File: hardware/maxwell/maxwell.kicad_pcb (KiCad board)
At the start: 2 copper layers, 124 x 60 mm, 81 parts, among them J1 Canbus 1, J10 SPI2_B, J11 BACKUP, J12 UART4, J13 UART5, J14 I2C1, J15 GPIO, J16 ESP_BM, J17 ESP_PROG, J18 Supercap, J2 Canbus 2, J3 Neopixel, J4 BOOT0, J5 SPI2_A, J6 Programmer, J7 Dynamo Input, J8 BOOT1, J9 Battery, Q1 BSS138, Q2 PSMN5R4-25YLD, Q3 NTR1P02T1, Q4 NTR1P02T1, Q5 NTR1P02T1, U1 MCP1501, U10 MIC39102, U2 SN65HVD233, U3 TPS2113, U5 ESP-32S, U7 STM32F103RETx, U8 TLP188, U9 Buck Regulator, Y1 32.768k, Y2 8M

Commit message: v1.5 ready for production.
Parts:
- removed C2: 2.2u, coddingtonbear:CP_Tantalum_Case-C_EIA-6032-28_Milling
- removed J15: GPIO, coddingtonbear:JST_XH_B03B-XH-A_03x2.50mm_Straight_LargePads
- removed J18: Supercap, coddingtonbear:JST_XH_B02B-XH-A_02x2.50mm_Straight_LargePads
- removed Q3: NTR1P02T1, coddingtonbear:SOT-23_LargePads
- added C15: 0.1u, coddingtonbear:0805_Milling, F.Cu at (88.4, 103.1)
- added C16: 0.1u, coddingtonbear:0805_Milling, F.Cu at (96.6, 118.7)
- added J19: Interconnect (Power), coddingtonbear:IDC-Header_2x08_P2.54mm_Vertical_Largepads, F.Cu at (92.6, 78.2)
- added J20: Interconnect (uC), coddingtonbear:IDC-Header_2x08_P2.54mm_Vertical_Largepads, F.Cu at (107.5, 78.4)
- added R26: 250, coddingtonbear:0805_Milling, F.Cu at (72.7, 94.3)
- added U11: SN74LVC1G14DBVR, Package_TO_SOT_SMD:SOT-23-5_HandSoldering, F.Cu at (80.6, 100.7)
- added U4: PCA9536D, coddingtonbear:SOIC-8_3.9x4.9mm_P1.27mm_LargePads, F.Cu at (86.4, 107.3)
- added U6: AD7995, Package_TO_SOT_SMD:SOT-23-8_Handsoldering, F.Cu at (92.9, 121.0)
- C1: value 2.2u -> 0.1u; footprint coddingtonbear:CP_Tantalum_Case-C_EIA-6032-28_Milling -> coddingtonbear:0805_Milling
- C17: footprint Capacitor_THT:CP_Radial_D13.0mm_P2.50mm -> coddingtonbear:JST_XH_B02B-XH-A_02x2.50mm_Straight_LargePads
- J2: value Canbus 2 -> SPI2_C; footprint coddingtonbear:JST_XH_B05B-XH-A_05x2.50mm_Straight_LargePads -> coddingtonbear:JST_XH_B06B-XH-A_06x2.50mm_Straight_LargePads
- R11: value 50 -> 10k
- R16, R2, R37, R7, R8: moved to F.Cu
- R18: value ANY -> 2k
- R25: value ANY -> 1k
- R3: value 500 -> 10k
- U7: footprint kicad-castellated-breakouts:QFP64-1.27MM-CASTELLATED-VERS -> kicad-castellated-breakouts:QFP64-1.27MM-CASTELLATED
- moved J2 83.2 mm to (174.8, 126.8), turned to 90 degrees
- moved BZ1 67.2 mm to (110.0, 125.0), turned to 0 degrees
- moved U1 60.6 mm to (86.9, 116.6), turned to 180 degrees
- moved C1 59.2 mm to (81.7, 115.0), turned to 90 degrees
- moved Q1 58.7 mm to (118.4, 127.0), turned to 270 degrees
- moved R4 52.9 mm to (118.5, 123.5), turned to 180 degrees
- moved R11 49.7 mm to (84.9, 113.1)
- moved R14 46.6 mm to (60.3, 121.9)
- moved D4 46.2 mm to (64.3, 117.2)
- moved C4 43.9 mm to (142.1, 84.3), turned to 225 degrees
- moved D1 43.4 mm to (65.1, 121.8)
- moved J3 37.4 mm to (132.7, 126.9)
- moved Q2 36.3 mm to (140.7, 126.6), turned to 90 degrees
- moved C10 36.2 mm to (130.7, 115.7), turned to 45 degrees
- moved J5 31.8 mm to (160.8, 126.8)
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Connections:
- net Net-(J9-Pad2) renamed /Power/BATT_PRE_POLARITY
- net Net-(Q4-Pad3) renamed /Power/BATT_CHARGE_PRE_POLARITY
- C1 pad 1: Net-(C1-Pad1) -> +3V3
- C1 pad 2: Net-(C1-Pad2) -> GND
- C17 pad 1: /Power/Batt_Charge -> /Power/+Dynamo_Buck
- C18 pad 2: /Power/Batt_Charge -> /Power/+Dynamo_Buck
- J2 pad 1: POWER_ON -> SPI2_CS_C
- J2 pad 3: /CAN+ -> SPI2_SCK
- J2 pad 4: /CAN- -> SPI2_MISO
- J2 pad 5: GND -> SPI2_MOSI
- Q5 pad 2: Net-(Q5-Pad2) -> /Power/BATT_PRE_SENSE
- R11 pad 1: Net-(C1-Pad2) -> ENABLE_VREF
- R11 pad 2: GND -> +3V3
- R18 pad 1: /Power/+Dynamo_Buck -> /Power/BATT_PRE_SENSE
- R18 pad 2: DYNAMO_BUCK_VOLTAGE -> ~BATT_DISABLE
- R20 pad 1: Net-(Q5-Pad2) -> /Power/BATT_PRE_SENSE
- R22 pad 2: Net-(Q5-Pad2) -> /Power/BATT_PRE_SENSE
- R25 pad 1: GND -> ~BATT_DISABLE
- R25 pad 2: DYNAMO_BUCK_VOLTAGE -> GND
- R3 pad 1: GND -> BATTERY_SOURCE_DISABLE
- U*1 pad 4: /Power/Batt_Charge -> /Power/+Dynamo_Buck
- U1 pad 1: Net-(C1-Pad1) -> Net-(U1-Pad1)
- U1 pad 4: +3V3 -> ENABLE_VREF
- U2 pad 5: Net-(U2-Pad5) -> (no net)
- U3 pad 1: Net-(U3-Pad1) -> POWER_SOURCE_INDICATOR
- U3 pad 3: DYNAMO_SOURCE_DISABLE -> BATTERY_SOURCE_DISABLE
- U3 pad 4: Net-(R3-Pad2) -> Net-(R26-Pad2)
- U3 pad 6: /Power/+Dynamo_Buck -> +BATT
- U3 pad 8: +BATT -> /Power/+Dynamo_Buck
- U5 pad 10: Net-(U5-Pad10) -> (no net)
- U5 pad 11: Net-(U5-Pad11) -> (no net)
- U5 pad 12: Net-(U5-Pad12) -> BT_DO
- U5 pad 13: Net-(U5-Pad13) -> BT_DI
- U5 pad 14: Net-(U5-Pad14) -> (no net)
- U5 pad 16: Net-(U5-Pad16) -> (no net)
- U5 pad 17: Net-(U5-Pad17) -> (no net)
- U5 pad 18: Net-(U5-Pad18) -> (no net)
- U5 pad 19: Net-(U5-Pad19) -> (no net)
- U5 pad 20: Net-(U5-Pad20) -> (no net)
- U5 pad 21: Net-(U5-Pad21) -> (no net)
- U5 pad 22: Net-(U5-Pad22) -> (no net)
- U5 pad 23: BT_DO -> (no net)
- U5 pad 24: BT_DI -> (no net)
- U5 pad 29: Net-(U5-Pad29) -> (no net)
- U5 pad 30: Net-(U5-Pad30) -> (no net)
- U5 pad 31: Net-(U5-Pad31) -> (no net)
- U5 pad 32: Net-(U5-Pad32) -> (no net)
- U5 pad 33: Net-(U5-Pad33) -> (no net)
- U5 pad 36: Net-(U5-Pad36) -> (no net)
- U5 pad 37: Net-(U5-Pad37) -> (no net)
- U5 pad 4: Net-(U5-Pad4) -> (no net)
- U5 pad 5: Net-(U5-Pad5) -> (no net)
- U5 pad 6: Net-(U5-Pad6) -> (no net)
- U5 pad 7: Net-(U5-Pad7) -> (no net)
- U5 pad 8: Net-(U5-Pad8) -> (no net)
- U5 pad 9: Net-(U5-Pad9) -> (no net)
- U7 pad 10: ~BATT_CHARGING -> (no net)
- U7 pad 11: CAN_DISABLE -> (no net)
- U7 pad 13: Net-(C1-Pad1) -> +3V3
- U7 pad 14: SPEED -> SPI2_CS_C
- U7 pad 15: DYNAMO_SOURCE_DISABLE -> SPI2_CS_B
- U7 pad 17: SPI2_CS_B -> BUZZER
- U7 pad 2: ~BATT_CHARGE_ENABLE -> (no net)
- U7 pad 20: Net-(U7-Pad20) -> (no net)
- U7 pad 21: Net-(U7-Pad21) -> (no net)
- U7 pad 22: Net-(U7-Pad22) -> (no net)
- U7 pad 24: DYNAMO_VOLTAGE -> ENABLE_BATT_POWER
- U7 pad 25: DYNAMO_BUCK_VOLTAGE -> (no net)
- U7 pad 26: ENABLE_BATT_POWER -> (no net)
- U7 pad 27: Net-(U7-Pad27) -> (no net)
- U7 pad 29: GPS_DI -> (no net)
- U7 pad 30: GPS_DO -> (no net)
- U7 pad 33: Net-(U7-Pad33) -> (no net)
- U7 pad 38: Net-(U7-Pad38) -> ~DISABLE_ESP
- U7 pad 39: Net-(U7-Pad39) -> (no net)
- U7 pad 40: Net-(U7-Pad40) -> (no net)
- U7 pad 41: Net-(U7-Pad41) -> (no net)
- U7 pad 44: ~DISABLE_ESP -> (no net)
- U7 pad 45: BUZZER -> (no net)
- U7 pad 50: POWER_ON -> (no net)
- U7 pad 55: Net-(J15-Pad1) -> POWER_ON
- U7 pad 56: Net-(J15-Pad2) -> CAN_DISABLE
- U7 pad 57: Net-(J15-Pad3) -> (no net)
- U7 pad 8: BATT_VOLTAGE -> SPEED
- U7 pad 9: CURRENT_SENSE -> (no net)
- Y1 pad 2: Net-(Y1-Pad2) -> (no net)
- Y1 pad 3: Net-(Y1-Pad3) -> (no net)
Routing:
- net GND: track 698.3 -> 808.6 mm, vias 12 -> 16
- net DYNAMO_SOURCE_DISABLE: track 89.6 -> 0.00 mm, vias 2 -> 0
- net ~BATT_CHARGE_ENABLE: track 86.4 -> 0.00 mm, vias 2 -> 0
- net ~BATT_CHARGING: track 100.9 -> 41.1 mm
- net CAN_DISABLE: track 78.6 -> 21.3 mm, vias 2 -> 0
- net I2C1_SDA: track 35.4 -> 84.2 mm
- net SPI2_CS_C: track 0.00 -> 48.6 mm
- net CAN_TX: track 56.8 -> 13.4 mm
- net BOOT0: track 92.8 -> 50.3 mm
- net SPI2_CS_A: track 69.2 -> 28.2 mm
- net CURRENT_SENSE: track 69.1 -> 29.2 mm, vias 0 -> 2
- net BATT_VOLTAGE: track 72.2 -> 36.7 mm, vias 0 -> 2
- net POWER_ON: track 60.6 -> 27.6 mm
- net CAN_RX: track 41.5 -> 12.0 mm
- net POWER_SOURCE_INDICATOR: track 0.00 -> 28.9 mm, vias 0 -> 2
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- removed copper zone on B.Cu, net GND
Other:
- board size 124 x 60 mm -> 122 x 59 mm
- net class Default: trace_width 0.4 -> 0.35; via_drill 0.4 -> 0.7
- net class Power added: clearance 0.2, trace_width 0.45, via_dia 2, via_drill 0.7
- board text added: "Maxwell v1.4 (Pwr) 2018-11-25 @coddingtonbear"
- board text added: "Maxwell v1.5 (uC) 2018-11-25 @coddingtonbear"
- board text removed: "+"
- board text removed: "-"
- board text removed: "0"
- board text removed: "1"
- board text removed: "4"
- board text removed: "5"
- board text removed: "A"
- board text removed: "B"
- board text removed: "C"
- board text removed: "CK"
- board text removed: "D"
- board text removed: "DI"
- board text removed: "DO"
- board text removed: "H"
- board text removed: "L"
- board text removed: "Maxwell v3.0 @coddingtonbear 24 June 2018"
- board text removed: "R"
- board text removed: "RX"
- board text removed: "T"
- board text removed: "TX"
- board text removed: "~"

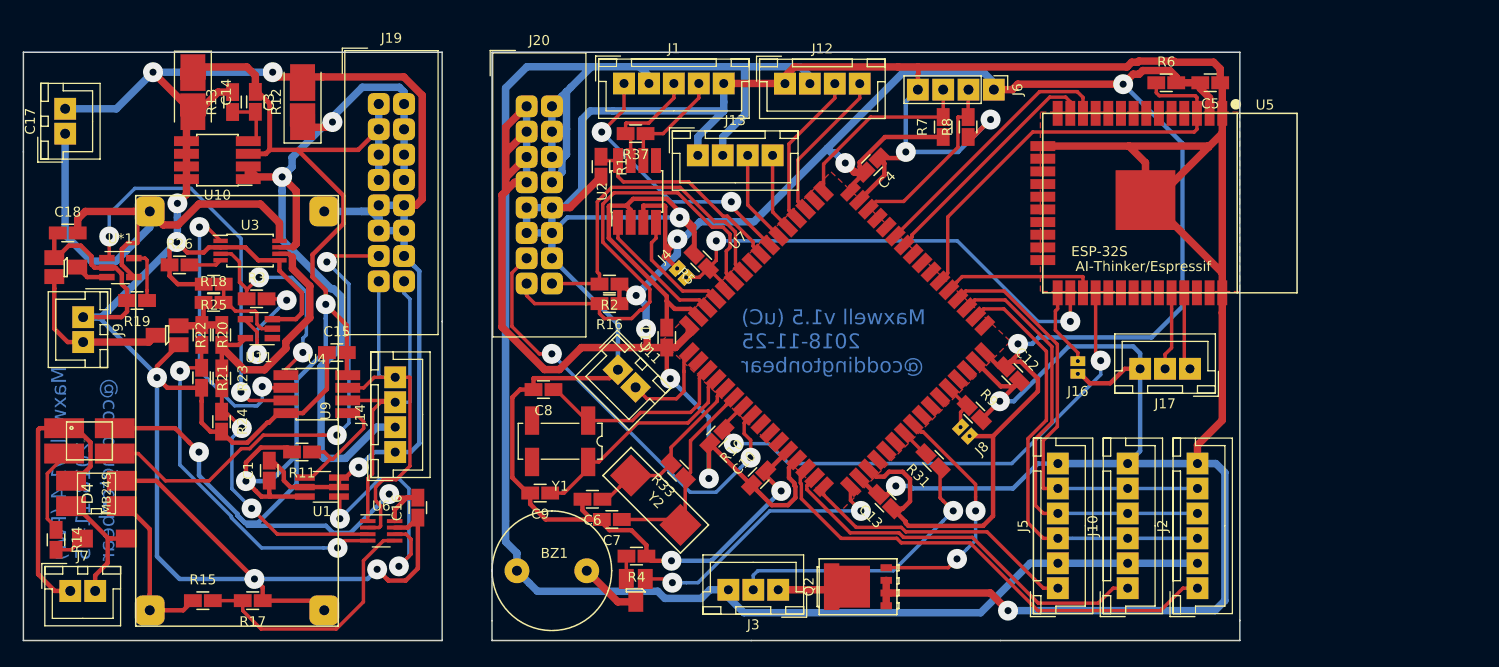
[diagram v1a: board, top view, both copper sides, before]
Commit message: Minor updates to mak certain pads slightly larger.
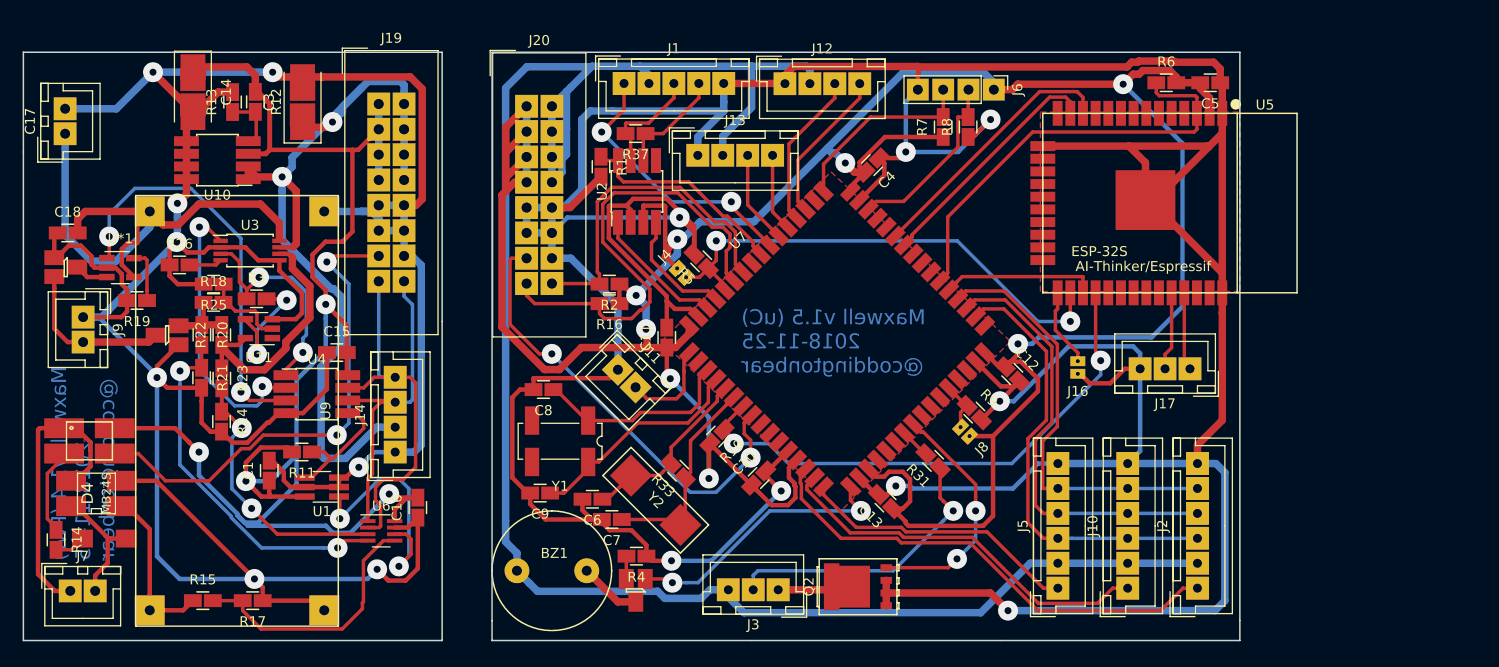
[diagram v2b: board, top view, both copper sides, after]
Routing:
- net VCC: track 278.2 -> 285.8 mm
- net GND: track 808.6 -> 811.0 mm
- net SPEED: track 94.1 -> 95.1 mm
- net I2C1_SDA: track 84.2 -> 85.1 mm
- net +3V3: track 455.1 -> 454.6 mm

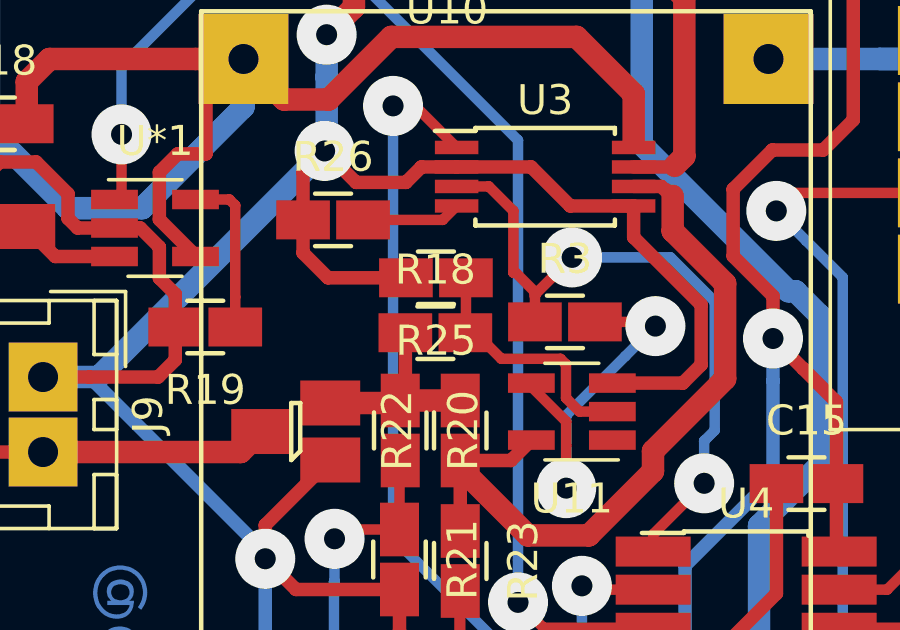
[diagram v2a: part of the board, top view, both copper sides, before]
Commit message: Switch to using diode drop instead of a voltage divider for controlling min battery power.
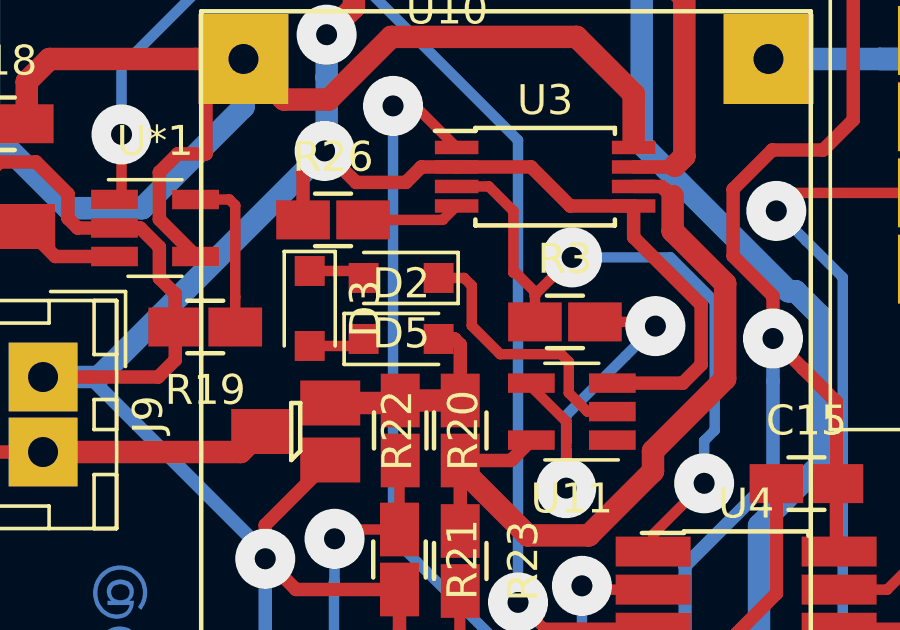
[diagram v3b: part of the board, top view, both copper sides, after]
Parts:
- removed R18: 2k, coddingtonbear:0805_Milling
- removed R25: 1k, coddingtonbear:0805_Milling
- added D2: 1N4148WS, Diode_SMD:D_SOD-323_HandSoldering, F.Cu at (74.9, 98.3)
- added D3: 1N4148WS, Diode_SMD:D_SOD-323_HandSoldering, F.Cu at (71.9, 97.3)
- added D5: 1N4148WS, Diode_SMD:D_SOD-323_HandSoldering, F.Cu at (74.9, 96.3)
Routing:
- net GND: track 811.0 -> 806.1 mm
- net Net-(D3-Pad1): track 0.00 -> 1.89 mm
- net Net-(D2-Pad1): track 0.00 -> 1.89 mm
- net ~BATT_DISABLE: track 8.49 -> 9.03 mm

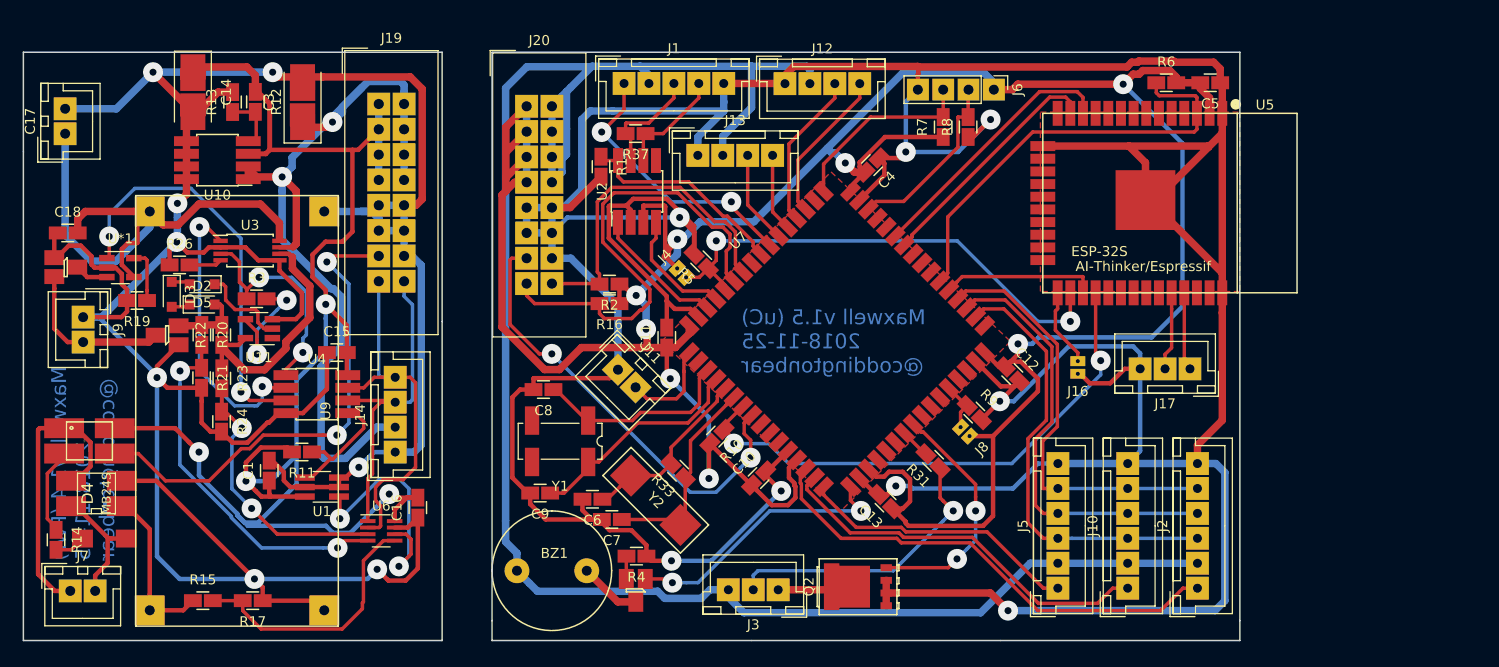
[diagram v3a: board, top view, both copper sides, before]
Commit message: Revision 1.6; switches to using an battery management IC for safety; adds better analog grounding.
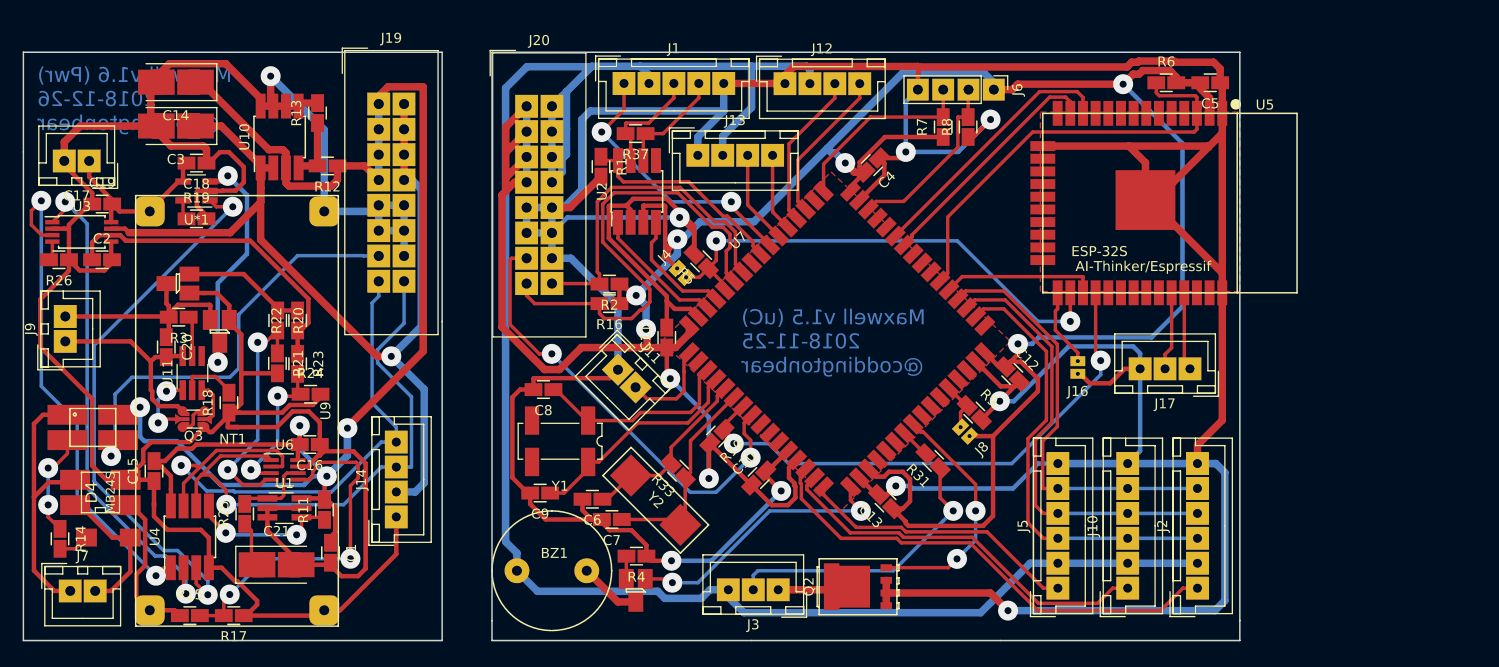
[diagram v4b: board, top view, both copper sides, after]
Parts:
- removed D2, D3, D5: 1N4148WS, Diode_SMD:D_SOD-323_HandSoldering
- added C19: 0.1u, coddingtonbear:0805_Milling, F.Cu at (64.9, 88.2)
- added C2: 0.1u, coddingtonbear:0805_Milling, F.Cu at (64.9, 93.8)
- added C20: 0.1u, coddingtonbear:0805_Milling, F.Cu at (71.3, 102.6)
- added C21: 2.2u, coddingtonbear:CP_Tantalum_Case-C_EIA-6032-28_Milling, F.Cu at (82.4, 124.4)
- added NT1: Net-Tie_2, NetTie:NetTie-2_SMD_Pad0.5mm, F.Cu at (78.0, 110.6)
- added Q3: DMN2400UV, coddingtonbear:SOT-563-LargePads, F.Cu at (74.1, 109.8)
- added R18: 2.7k, coddingtonbear:0805_Milling, F.Cu at (77.6, 108.2)
- added R25: 50, coddingtonbear:0805_Milling, F.Cu at (79.2, 119.3)
- R3: value 10k -> 330
- U11: value SN74LVC1G14DBVR -> AP9101C; footprint Package_TO_SOT_SMD:SOT-23-5_HandSoldering -> Package_TO_SOT_SMD:TSOT-23-6_HandSoldering
- U6: value AD7995 -> AD7991
- moved C15 21.9 mm to (70.1, 115.0), turned to 90 degrees
- moved U4 19.2 mm to (73.7, 121.6), turned to 90 degrees
- moved U3 17.0 mm to (62.9, 91.0)
- moved Q4 16.7 mm to (76.7, 101.0), turned to 270 degrees
- moved C18 14.7 mm to (74.4, 84.1), turned to 180 degrees
- moved C3 12.9 mm to (72.3, 80.4), turned to 180 degrees
- moved C16 12.5 mm to (85.7, 112.3), turned to 180 degrees
- moved R26 12.1 mm to (60.6, 93.8), turned to 180 degrees
- moved U6 11.5 mm to (83.2, 114.9)
- moved U*1 10.8 mm to (74.4, 86.9), turned to 180 degrees
- moved C1 10.3 mm to (87.8, 123.2), turned to 270 degrees
- moved R19 10.1 mm to (74.4, 89.7), turned to 0 degrees
- moved R12 9.67 mm to (87.5, 84.4), turned to 180 degrees
- moved R24 9.34 mm to (85.8, 107.3), turned to 0 degrees
- moved R13 8.59 mm to (86.5, 79.1)
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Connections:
- C1 pad 2: GND -> GNDA
- C16 pad 1: GND -> GNDA
- J9 pad 1: GND -> /Power/BATT_PRE_PROT
- R3 pad 1: BATTERY_SOURCE_DISABLE -> Net-(R3-Pad1)
- R3 pad 2: Net-(R3-Pad2) -> /Power/BATT_PRE_POLARITY
- U1 pad 2: GND -> GNDA
- U1 pad 3: GND -> GNDA
- U1 pad 5: GND -> GNDA
- U11 pad 1: (no net) -> Net-(Q3-Pad5)
- U11 pad 2: ~BATT_DISABLE -> Net-(R18-Pad2)
- U11 pad 3: GND -> Net-(Q3-Pad2)
- U11 pad 4: Net-(R3-Pad2) -> (no net)
- U11 pad 5: +BATT -> Net-(R3-Pad1)
- U2 pad 5: (no net) -> Net-(U2-Pad5)
- U3 pad 3: BATTERY_SOURCE_DISABLE -> DISABLE_BATTERY_SRC
- U4 pad 1: BATTERY_SOURCE_DISABLE -> DISABLE_BATTERY_SRC
- U5 pad 10: (no net) -> Net-(U5-Pad10)
- U5 pad 11: (no net) -> Net-(U5-Pad11)
- U5 pad 14: (no net) -> Net-(U5-Pad14)
- U5 pad 16: (no net) -> Net-(U5-Pad16)
- U5 pad 17: (no net) -> Net-(U5-Pad17)
- U5 pad 18: (no net) -> Net-(U5-Pad18)
- U5 pad 19: (no net) -> Net-(U5-Pad19)
- U5 pad 20: (no net) -> Net-(U5-Pad20)
- U5 pad 21: (no net) -> Net-(U5-Pad21)
- U5 pad 22: (no net) -> Net-(U5-Pad22)
- U5 pad 23: (no net) -> Net-(U5-Pad23)
- U5 pad 24: (no net) -> Net-(U5-Pad24)
- U5 pad 29: (no net) -> Net-(U5-Pad29)
- U5 pad 30: (no net) -> Net-(U5-Pad30)
- U5 pad 31: (no net) -> Net-(U5-Pad31)
- U5 pad 32: (no net) -> Net-(U5-Pad32)
- U5 pad 33: (no net) -> Net-(U5-Pad33)
- U5 pad 36: (no net) -> Net-(U5-Pad36)
- U5 pad 37: (no net) -> Net-(U5-Pad37)
- U5 pad 4: (no net) -> Net-(U5-Pad4)
- U5 pad 5: (no net) -> Net-(U5-Pad5)
- U5 pad 6: (no net) -> Net-(U5-Pad6)
- U5 pad 7: (no net) -> Net-(U5-Pad7)
- U5 pad 8: (no net) -> Net-(U5-Pad8)
- U5 pad 9: (no net) -> Net-(U5-Pad9)
- U6 pad 7: GND -> GNDA
- U7 pad 10: (no net) -> Net-(U7-Pad10)
- U7 pad 11: (no net) -> Net-(U7-Pad11)
- U7 pad 2: (no net) -> Net-(U7-Pad2)
- U7 pad 20: (no net) -> Net-(U7-Pad20)
- U7 pad 21: (no net) -> Net-(U7-Pad21)
- U7 pad 22: (no net) -> Net-(U7-Pad22)
- U7 pad 25: (no net) -> Net-(U7-Pad25)
- U7 pad 26: (no net) -> Net-(U7-Pad26)
- U7 pad 27: (no net) -> Net-(U7-Pad27)
- U7 pad 29: (no net) -> Net-(U7-Pad29)
- U7 pad 30: (no net) -> Net-(U7-Pad30)
- U7 pad 33: (no net) -> Net-(U7-Pad33)
- U7 pad 39: (no net) -> Net-(U7-Pad39)
- U7 pad 40: (no net) -> Net-(U7-Pad40)
- U7 pad 41: (no net) -> Net-(U7-Pad41)
- U7 pad 44: (no net) -> Net-(U7-Pad44)
- U7 pad 45: (no net) -> Net-(U7-Pad45)
- U7 pad 50: (no net) -> Net-(U7-Pad50)
- U7 pad 57: (no net) -> Net-(U7-Pad57)
- U7 pad 9: (no net) -> Net-(U7-Pad9)
- Y1 pad 2: (no net) -> Net-(Y1-Pad2)
- Y1 pad 3: (no net) -> Net-(Y1-Pad3)
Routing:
- net GND: track 806.1 -> 723.9 mm, vias 16 -> 9
- net DISABLE_BATTERY_SRC: track 0.00 -> 49.5 mm, vias 0 -> 2
- net GNDA: track 0.00 -> 49.3 mm
- net /Power/+Dynamo_Buck: track 57.3 -> 17.9 mm
- net I2C1_SCL: track 66.6 -> 90.8 mm, vias 0 -> 1
- net BATTERY_SOURCE_DISABLE: track 22.6 -> 0.00 mm, vias 2 -> 0
- net I2C1_SDA: track 85.1 -> 107.6 mm, vias 0 -> 1
- net /Power/BATT_CHARGE_PRE_POLARITY: track 3.39 -> 24.8 mm, vias 0 -> 2
- net POWER_SOURCE_INDICATOR: track 28.9 -> 50.2 mm
- net /Power/BATT_PRE_PROT: track 0.00 -> 20.8 mm
- net Net-(R25-Pad2): track 24.5 -> 7.76 mm, vias 2 -> 0
- net ~BATT_CHARGING: track 41.1 -> 56.0 mm
- net CURRENT_SENSE: track 29.2 -> 15.2 mm
- net Net-(R3-Pad2): track 13.3 -> 0.00 mm, vias 2 -> 0
- net BATT_VOLTAGE: track 36.7 -> 24.0 mm
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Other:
- board text added: "Maxwell v1.6 (Pwr) 2018-12-26 @coddingtonbear"
- board text removed: "Maxwell v1.4 (Pwr) 2018-11-25 @coddingtonbear"
